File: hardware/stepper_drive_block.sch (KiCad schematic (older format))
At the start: 25 parts, among them J2001 Stepper Motor, P2001 CONN_01X04, U2001 L6470

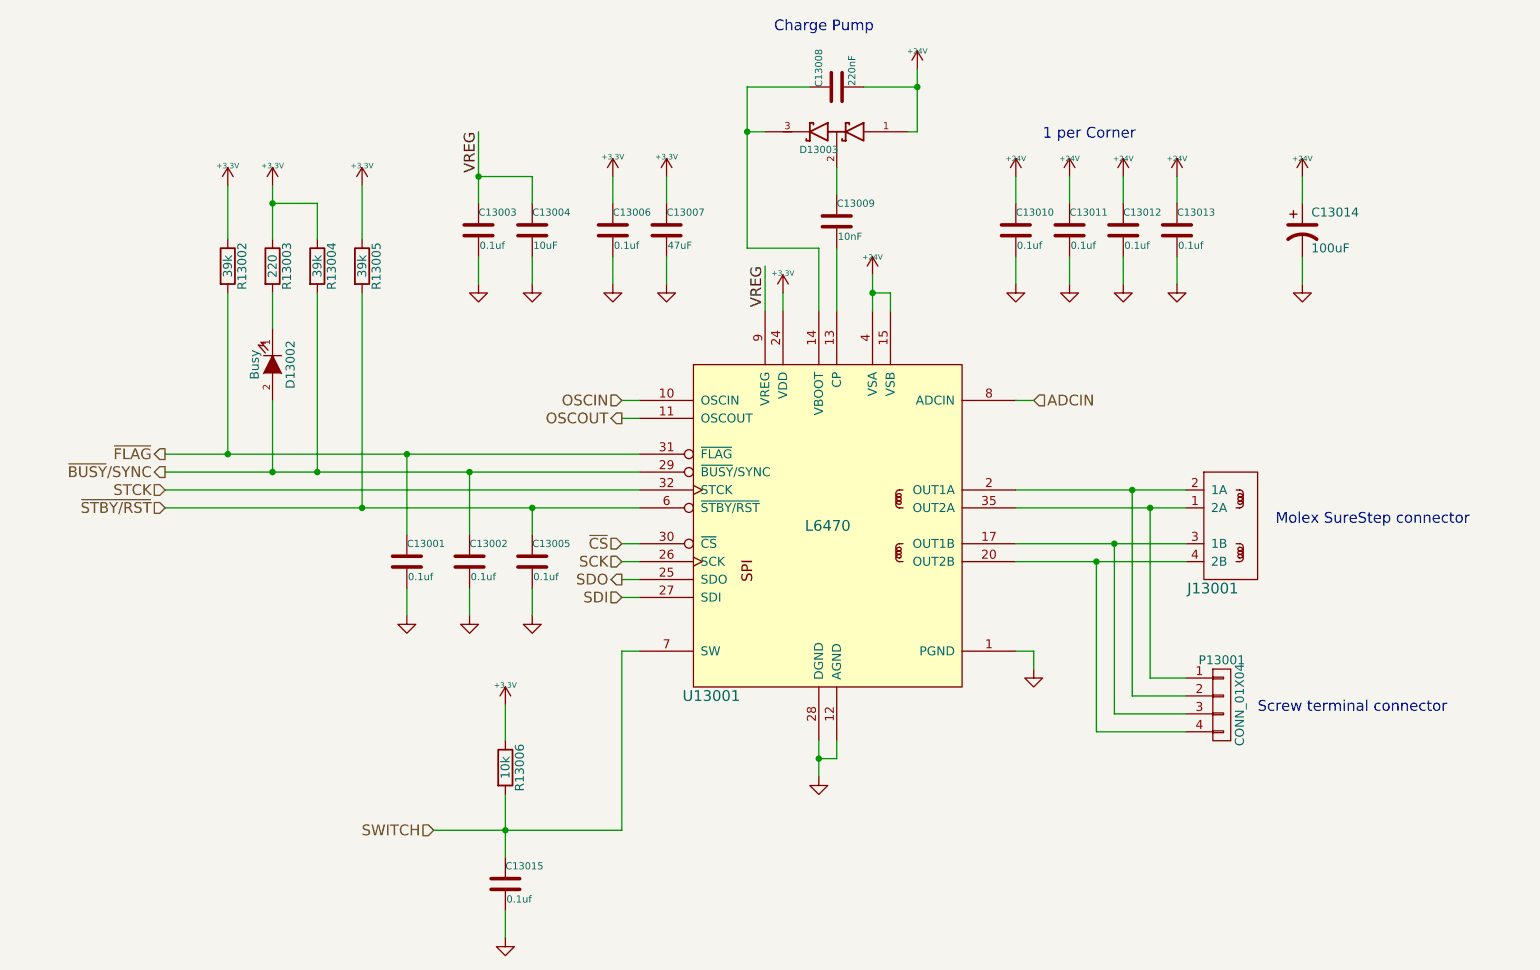
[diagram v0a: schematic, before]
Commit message: added some new part numbers
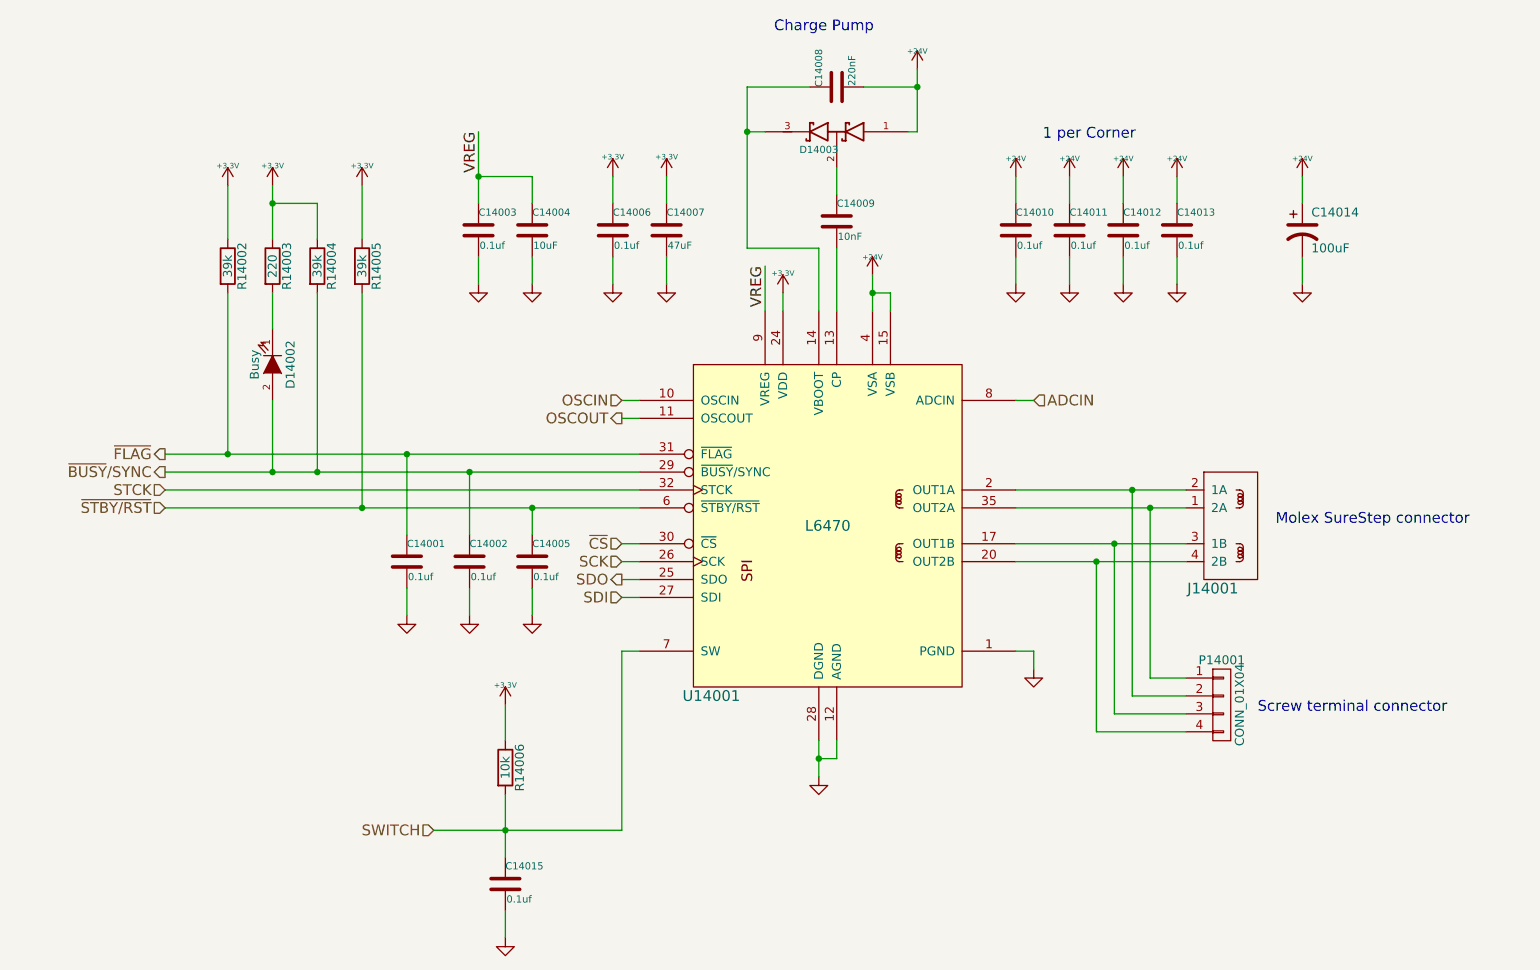
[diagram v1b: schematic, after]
